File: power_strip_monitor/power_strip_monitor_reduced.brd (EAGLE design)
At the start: 80 x 55 mm, 74 parts, among them Q1 4.096MHz, U1 CS5467, U2 CS5467, U4 ATMEGA168, U5 RAC01_02-SC, U6 XBEE-1B1

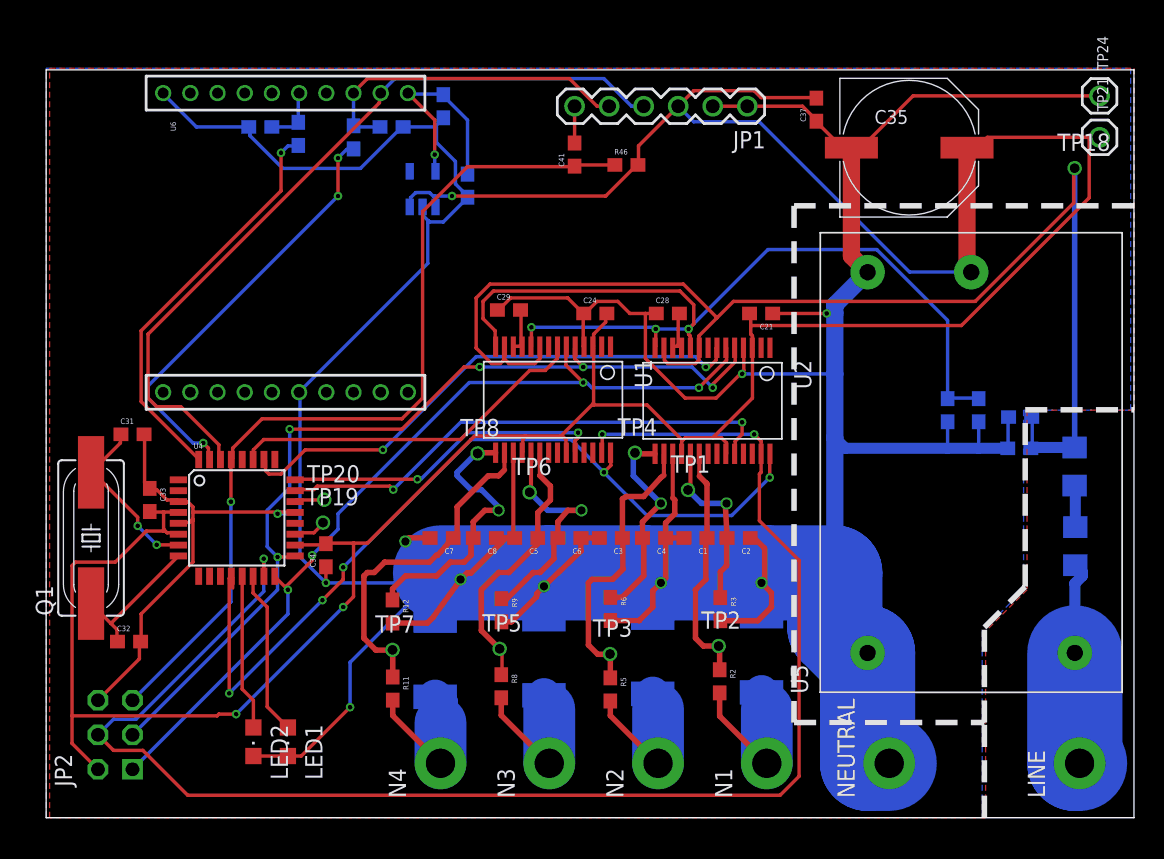
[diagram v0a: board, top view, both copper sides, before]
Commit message: Added DRC rules, second LINE hole
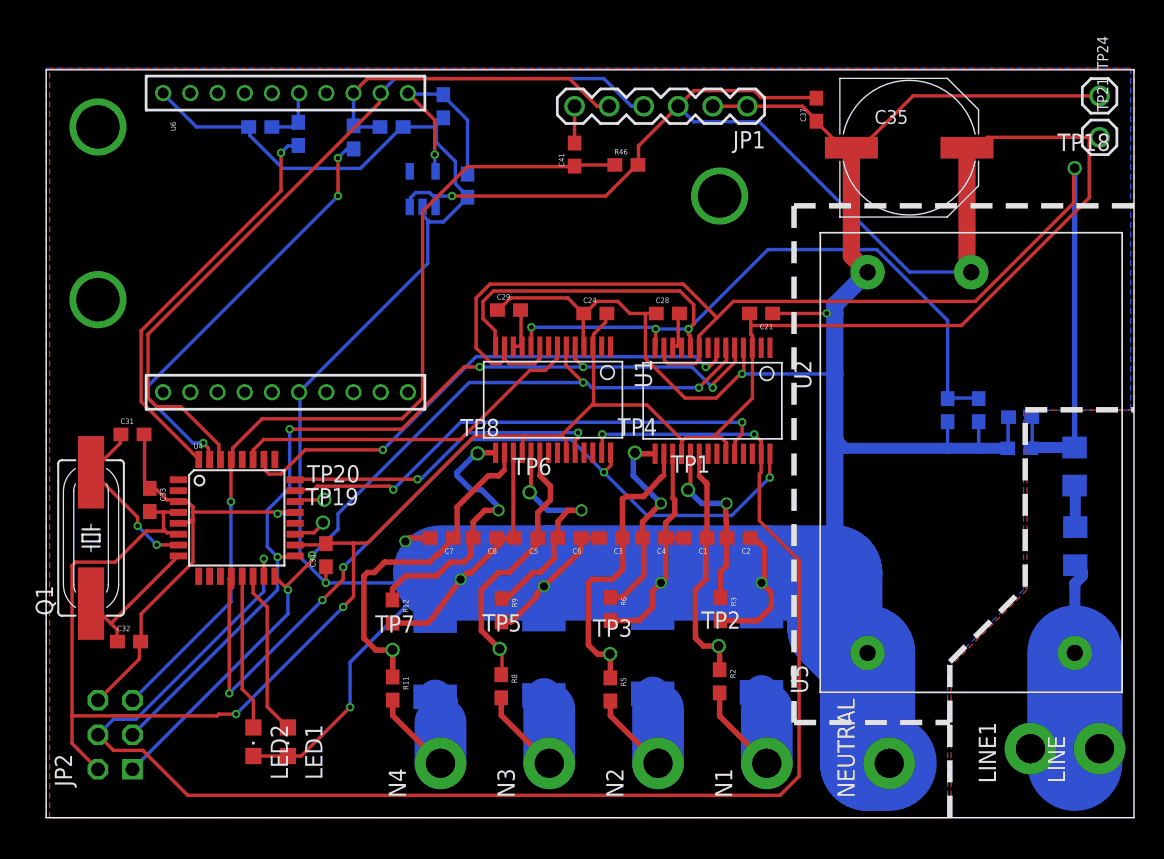
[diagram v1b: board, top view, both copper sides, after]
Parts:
- added LINE1: 1P_HOLE, Cool_Electricity:14GAUGE_HOLE
- moved LINE 1.82 mm to (77.5, 5.08)
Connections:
- net HOT: now also LINE1.P$1
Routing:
- net HOT: track 15.4 -> 21.2 mm
- net GND: vias 10 -> 13
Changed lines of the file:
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@@
 <?xml version="1.0" encoding="utf-8"?>
 <!DOCTYPE eagle SYSTEM "eagle.dtd">
-<eagle version="6.2">
+<eagle version="6.1">
 <drawing>
 <settings>
@@
 <setting verticaltext="up"/>
 </settings>
-<grid distance="0.01" unitdist="inch" unit="inch" style="lines" multiple="1" display="yes" altdistance="0.1" altunitdist="mm" altunit="mm"/>
+<grid distance="0.1" unitdist="inch" unit="inch" style="lines" multiple="1" display="yes" altdistance="0.05" altunitdist="inch" altunit="inch"/>
 <layers>
 <layer number="1" name="Top" color="4" fill="1" visible="yes" active="yes"/>
@@
 <wire x1="80" y1="55" x2="0" y2="55" width="0" layer="20"/>
 <wire x1="0" y1="55" x2="0" y2="0" width="0" layer="20"/>
-<wire x1="69" y1="0" x2="69" y2="7" width="0.4064" layer="21" style="shortdash"/>
-<wire x1="69" y1="7" x2="69" y2="14" width="0.4064" layer="21" style="shortdash"/>
-<wire x1="69" y1="14" x2="72" y2="17" width="0.4064" layer="21" style="shortdash"/>
+<wire x1="66.46" y1="0" x2="66.46" y2="7" width="0.4064" layer="21" style="shortdash"/>
+<wire x1="66.46" y1="7" x2="66.46" y2="11.46" width="0.4064" layer="21" style="shortdash"/>
+<wire x1="66.46" y1="11.46" x2="72" y2="17" width="0.4064" layer="21" style="shortdash"/>
 <wire x1="72" y1="17" x2="72" y2="30" width="0.4064" layer="21" style="shortdash"/>
 <wire x1="72" y1="30" x2="80" y2="30" width="0.4064" layer="21" style="shortdash"/>
 <wire x1="80" y1="45" x2="55" y2="45" width="0.4064" layer="21" style="shortdash"/>
 <wire x1="55" y1="45" x2="55" y2="7" width="0.4064" layer="21" style="shortdash"/>
-<wire x1="55" y1="7" x2="69" y2="7" width="0.4064" layer="21" style="shortdash"/>
+<wire x1="55" y1="7" x2="66.46" y2="7" width="0.4064" layer="21" style="shortdash"/>
 <wire x1="75.6" y1="12.2" x2="75.8" y2="12.2" width="6.4516" layer="30"/>
 <wire x1="75.8" y1="12.2" x2="75.8" y2="4" width="6.4516" layer="30"/>
@@
 <element name="C35" library="rcl_new" package="PANASONIC_G" value="1000u" x="63.47" y="49.275"/>
 <element name="U7" library="Cool_Electricity" package="TSOT23-5_LINEAR" value="" x="27.686" y="46.228" rot="MR0"/>
-<element name="LINE" library="Cool_Electricity" package="14GAUGE_HOLE" value="1P_HOLE" x="76" y="4"/>
+<element name="LINE" library="Cool_Electricity" package="14GAUGE_HOLE" value="1P_HOLE" x="77.47" y="5.08"/>
 <element name="NEUTRAL" library="Cool_Electricity" package="14GAUGE_HOLE" value="1P_HOLE" x="62" y="4"/>
 <element name="N1" library="Cool_Electricity" package="14GAUGE_HOLE" value="1P_HOLE" x="53" y="4"/>
@@
 <element name="LED1" library="led" package="CHIPLED_0805" value="" x="17.78" y="5.588" rot="R180"/>
 <element name="LED2" library="led" package="CHIPLED_0805" value="" x="15.24" y="5.588" rot="R180"/>
+<element name="LINE1" library="Cool_Electricity" package="14GAUGE_HOLE" value="1P_HOLE" x="72.39" y="5.08"/>
 </elements>
 <signals>
@@
 <vertex x="79.756" y="29.972"/>
 <vertex x="71.882" y="29.972"/>
-<vertex x="71.882" y="17.272"/>
 <vertex x="71.882" y="16.764"/>
-<vertex x="68.834" y="13.716"/>
-<vertex x="68.834" y="0"/>
-<vertex x="5.842" y="0"/>
+<vertex x="66.294" y="11.176"/>
+<vertex x="66.294" y="0"/>
 </polygon>
 <polygon width="0.4064" layer="1" isolate="0.508">
@@
 <vertex x="80.01" y="29.972"/>
 <vertex x="72.136" y="29.972"/>
-<vertex x="72.136" y="17.272"/>
 <vertex x="72.136" y="16.764"/>
-<vertex x="69.088" y="13.716"/>
-<vertex x="69.088" y="0"/>
-<vertex x="6.096" y="0"/>
+<vertex x="66.548" y="11.176"/>
+<vertex x="66.548" y="0"/>
 </polygon>
 <contactref element="LED1" pad="C"/>
@@
 <wire x1="27.178" y1="16.256" x2="28.356" y2="16.256" width="0.254" layer="16"/>
 <wire x1="28.356" y1="16.256" x2="28.61" y2="16.51" width="0.254" layer="16"/>
+<via x="3.81" y="50.8" extent="1-16" drill="3.2"/>
+<via x="3.81" y="38.1" extent="1-16" drill="3.2"/>
+<via x="49.53" y="45.72" extent="1-16" drill="3.2"/>
 </signal>
 <signal name="NRET2">
@@
 <contactref element="U5" pad="2"/>
 <contactref element="LINE" pad="P$1"/>
-<wire x1="76" y1="4" x2="75.65" y2="4" width="7" layer="16"/>
-<wire x1="75.65" y1="4" x2="75.65" y2="12.12" width="7" layer="16"/>
+<wire x1="75.65" y1="4" x2="75.65" y2="5.08" width="7" layer="16"/>
+<wire x1="75.65" y1="5.08" x2="75.65" y2="12.12" width="7" layer="16"/>
 <wire x1="75.65" y1="12.12" x2="75.65" y2="17.23" width="0.8128" layer="16"/>
 <wire x1="75.65" y1="17.23" x2="76.2" y2="17.78" width="0.8128" layer="16"/>
 <wire x1="76.2" y1="17.78" x2="76.2" y2="18.058" width="0.8128" layer="16"/>
 <wire x1="76.2" y1="18.058" x2="75.686" y2="18.572" width="0.8128" layer="16"/>
+<contactref element="LINE1" pad="P$1"/>
+<wire x1="72.39" y1="5.08" x2="75.65" y2="5.08" width="0.4064" layer="16"/>
+<wire x1="77.47" y1="5.08" x2="76.2" y2="5.08" width="0.4064" layer="16"/>
+<wire x1="75.65" y1="4" x2="76.2" y2="4" width="0.4064" layer="16"/>
+<wire x1="76.2" y1="4" x2="76.2" y2="5.08" width="0.4064" layer="16"/>
 </signal>
 <signal name="N$2">

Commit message: Added plastic mount
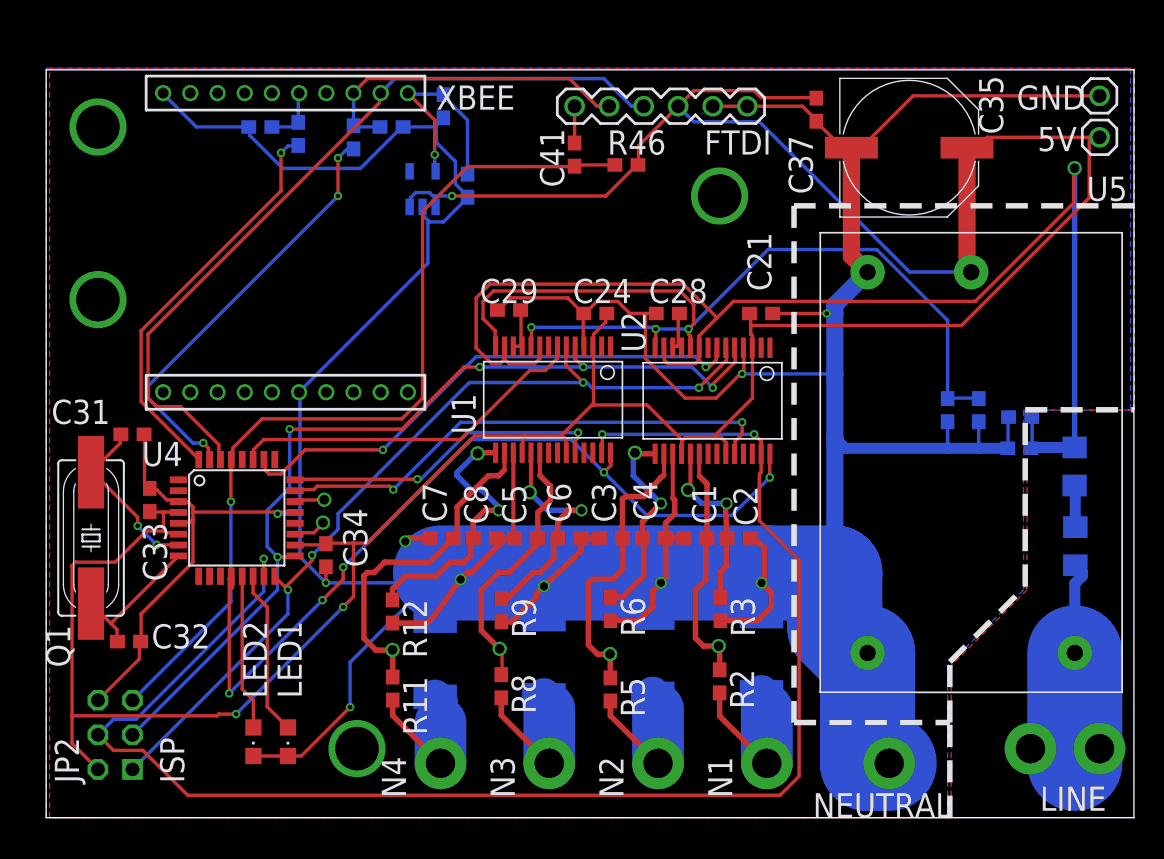
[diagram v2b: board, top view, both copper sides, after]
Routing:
- net GND: vias 13 -> 14
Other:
- board text added: "5V"
- board text added: "DANGER"
- board text added: "FTDI"
- board text added: "GND"
- board text added: "ISP"
- board text added: "Jimmy Wu"
- board text added: "Kevin Weekly"
- board text added: "Never plug in"
- board text added: "Power Strip Monitor"
- board text added: "XBEE"
- board text added: "computer while"
- board text added: "mains connected"
